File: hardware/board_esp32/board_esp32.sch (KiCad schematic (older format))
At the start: 96 parts, among them J1 USB_B_Micro, J2 Conn_01x02, J3 Micro_SD_Card_Det_Hirose_DM3AT, Q1 AO3401, Q2 AO3400, Q3 AO3401, SW1 SW_Push, U1 FT231XS, U2 ESP32-WROOM-32D, U3 E22-900M22S, U4 E22-900M30S, U5 TPS62162DGK

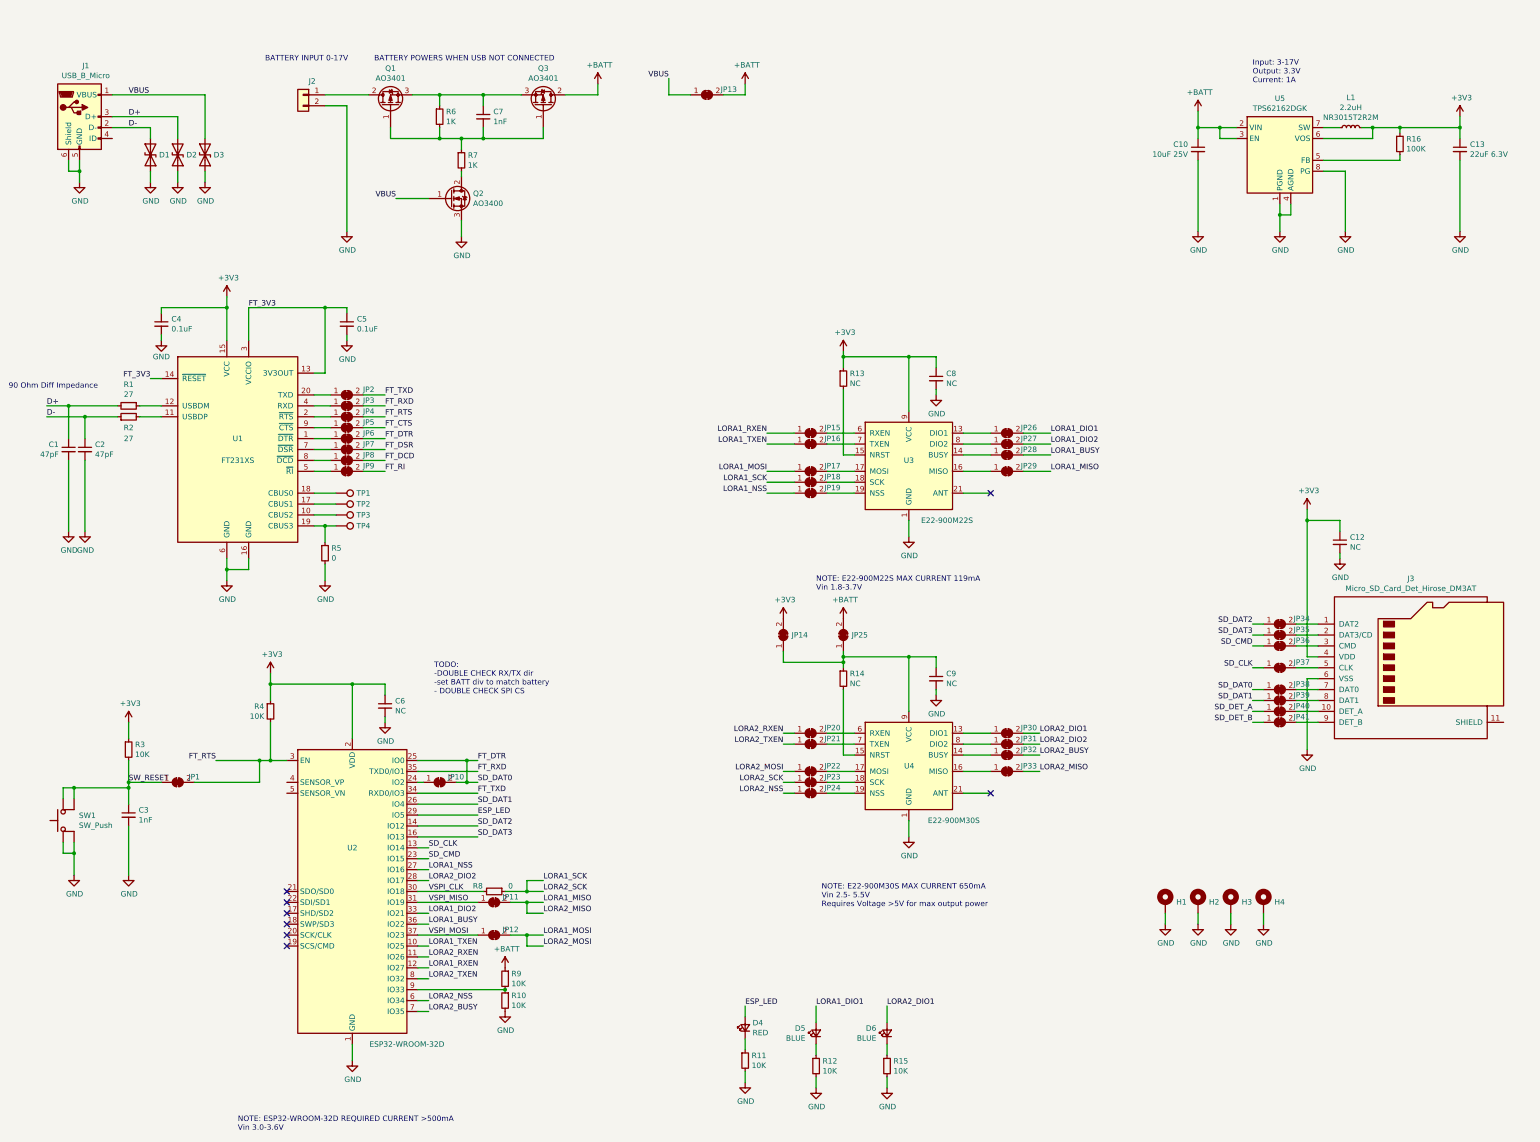
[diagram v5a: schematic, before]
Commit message: finishes up layout of board_esp32
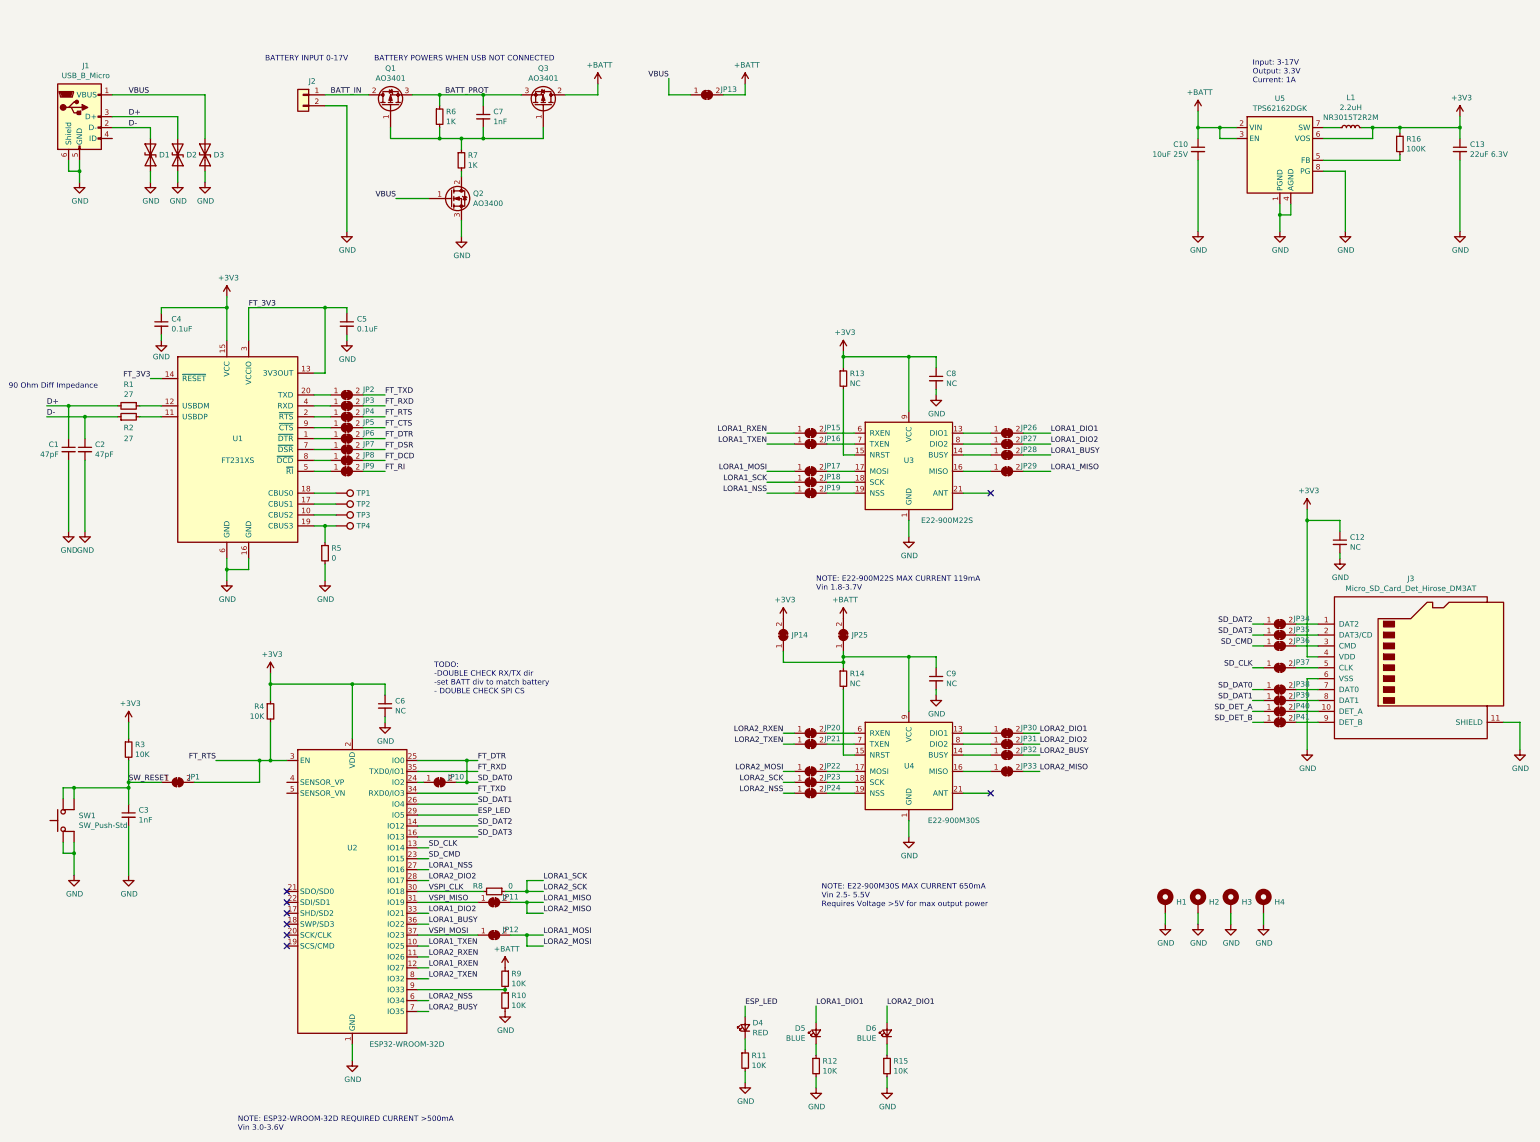
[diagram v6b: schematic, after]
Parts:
- removed SW1: SW_Push, Button_Switch_SMD:SW_Push_1P1T-SH_NO_CK_KMR2xxG, symbol board_esp32-rescue:SW_Push-symbols
- added SW1: SW_Push-Std, Button_Switch_SMD:SW_Push_1P1T-SH_NO_CK_KMR2xxG, symbol symbols:SW_Push-Std
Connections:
- net GND: now also J3.11 (SHIELD), SW1.1
- net SW_RESET: now also SW1.2, SW1.4
- net BATT_IN: now reaches J2.1 (Pin_1), Q1.2 (D)
- net BATT_PROT: now reaches C7.1, Q1.3 (S), Q3.3 (S), R6.1
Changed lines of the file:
@@
-	1    0    0    -1
-$EndComp
-$Comp
-L Device:C_Small C10
-U 1 1 5DCE2BB3
-P 11500 1550
-F 0 "C10" H 11408 1596 50  0000 R CNN
-F 1 "10uF 25V" H 11408 1505 50  0000 R CNN
-F 2 "Capacitor_SMD:C_0805_2012Metric" H 11500 1550 50  0001 C CNN
-F 3 "~" H 11500 1550 50  0001 C CNN
-	1    11500 1550
 	1    0    0    -1
 $EndComp
@@
 	1700 7350 1700 7150
 Wire Wire Line
-	1200 8000 1200 7900
-Wire Wire Line
 	1700 7400 1700 7350
 Wire Wire Line
@@
 Wire Wire Line
 	1700 7550 1700 7400
-$Comp
-L board_esp32-rescue:SW_Push-symbols SW1
-U 1 1 5DCB83D3
-P 1100 7700
-F 0 "SW1" V 1146 7556 50  0000 R CNN
-F 1 "SW_Push" V 1055 7556 50  0000 R CNN
-F 2 "Button_Switch_SMD:SW_Push_1P1T-SH_NO_CK_KMR2xxG" H 1100 7900 50  0001 C CNN
-F 3 "" H 1100 7900 50  0001 C CNN
-	1    1100 7700
-	0    -1   -1   0
-$EndComp
 $Comp
 L Device:R_Small R3
@@
 	1    0    0    -1
 $EndComp
-Wire Wire Line
-	1200 7500 1200 7400
 $Comp
 L power:GND #PWR0128
@@
 $EndComp
 Wire Wire Line
-	1100 7400 1100 7500
-Wire Wire Line
 	1200 8000 1200 8200
-Wire Wire Line
-	1100 7900 1100 8000
 Wire Wire Line
 	1700 7350 2000 7350
@@
 Text Label 4450 8250 0    50   ~ 0
 LORA2_DIO2
+Wire Wire Line
+	14300 6800 14450 6800
+Wire Wire Line
+	14450 6800 14450 7050
+$Comp
+L power:GND #PWR0147
+U 1 1 5E17CB00
+P 14450 7050
+F 0 "#PWR0147" H 14450 6800 50  0001 C CNN
+F 1 "GND" H 14455 6877 50  0000 C CNN
+F 2 "" H 14450 7050 50  0001 C CNN
+F 3 "" H 14450 7050 50  0001 C CNN
+	1    14450 7050
+	1    0    0    -1
+$EndComp
+$Comp
+L Device:C_Small C10
+U 1 1 5DCE2BB3
+P 11500 1550
+F 0 "C10" H 11408 1596 50  0000 R CNN
+F 1 "10uF 25V" H 11408 1505 50  0000 R CNN
+F 2 "Capacitor_SMD:C_0805_2012Metric" H 11500 1550 50  0001 C CNN
+F 3 "~" H 11500 1550 50  0001 C CNN
+	1    11500 1550
+	1    0    0    -1
+$EndComp
+Text Label 3550 1050 0    50   ~ 0
+BATT_IN
+Text Label 4600 1050 0    50   ~ 0
+BATT_PROT
+Wire Wire Line
+	1200 8000 1200 7900
+Wire Wire Line
+	1200 7500 1200 7400
+Wire Wire Line
+	1100 7400 1100 7500
+Wire Wire Line
+	1100 7900 1100 8000
+$Comp
+L symbols:SW_Push-Std SW1
+U 1 1 5E1D81ED
+P 1100 7700
+F 0 "SW1" V 1145 7557 50  0000 R CNN
+F 1 "SW_Push-Std" V 1055 7557 50  0000 R CNN
+F 2 "Button_Switch_SMD:SW_Push_1P1T-SH_NO_CK_KMR2xxG" H 1100 7900 50  0001 C CNN
+F 3 "" H 1100 7900 50  0001 C CNN
+	1    1100 7700
+	0    -1   -1   0
+$EndComp
 $EndSCHEMATC

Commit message: add a few more vias and generates GERBERs for board_esp32
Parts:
- U5: footprint Package_SO:MSOP-8_3x3mm_P0.65mm -> parts:MSOP-8_3x3mm_P0.65mm

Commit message: updates board_esp32 to fix manufacture issue with annular ring size
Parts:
- H1, H2, H3, H4: footprint MountingHole:MountingHole_2.2mm_M2 -> MountingHole:MountingHole_2.2mm_M2_ISO7380_Pad
